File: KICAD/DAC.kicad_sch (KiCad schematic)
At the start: 34 parts, among them IC4 PCM5102AQPWRQ1, IC6 PCM5102AQPWRQ1

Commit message: clear
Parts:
- IC4, IC6: footprint Package_SO:TSSOP-20_4.4x6.5mm_P0.65mm -> footprints:PCM5102AQPWRQ1
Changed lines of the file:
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@@
 			)
 		)
-		(property "Footprint" "Package_SO:TSSOP-20_4.4x6.5mm_P0.65mm"
+		(property "Footprint" "footprints:PCM5102AQPWRQ1"
 			(at 101.6 47.32 0)
 			(hide yes)
@@
 			)
 		)
-		(property "Footprint" "Package_SO:TSSOP-20_4.4x6.5mm_P0.65mm"
+		(property "Footprint" "footprints:PCM5102AQPWRQ1"
 			(at 100.33 -6.02 0)
 			(hide yes)

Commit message: Verification PCM5102A
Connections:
- net GND: now also IC6.12 (SCK)
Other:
- note added: "c'est parfait mec, il manquait juste un fil entre SCK et GND sur un des PCM5102A"
- moved on the sheet: C54, C57, C58, C59, C60, C61, C62, C63, C64, C65, C66, C67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

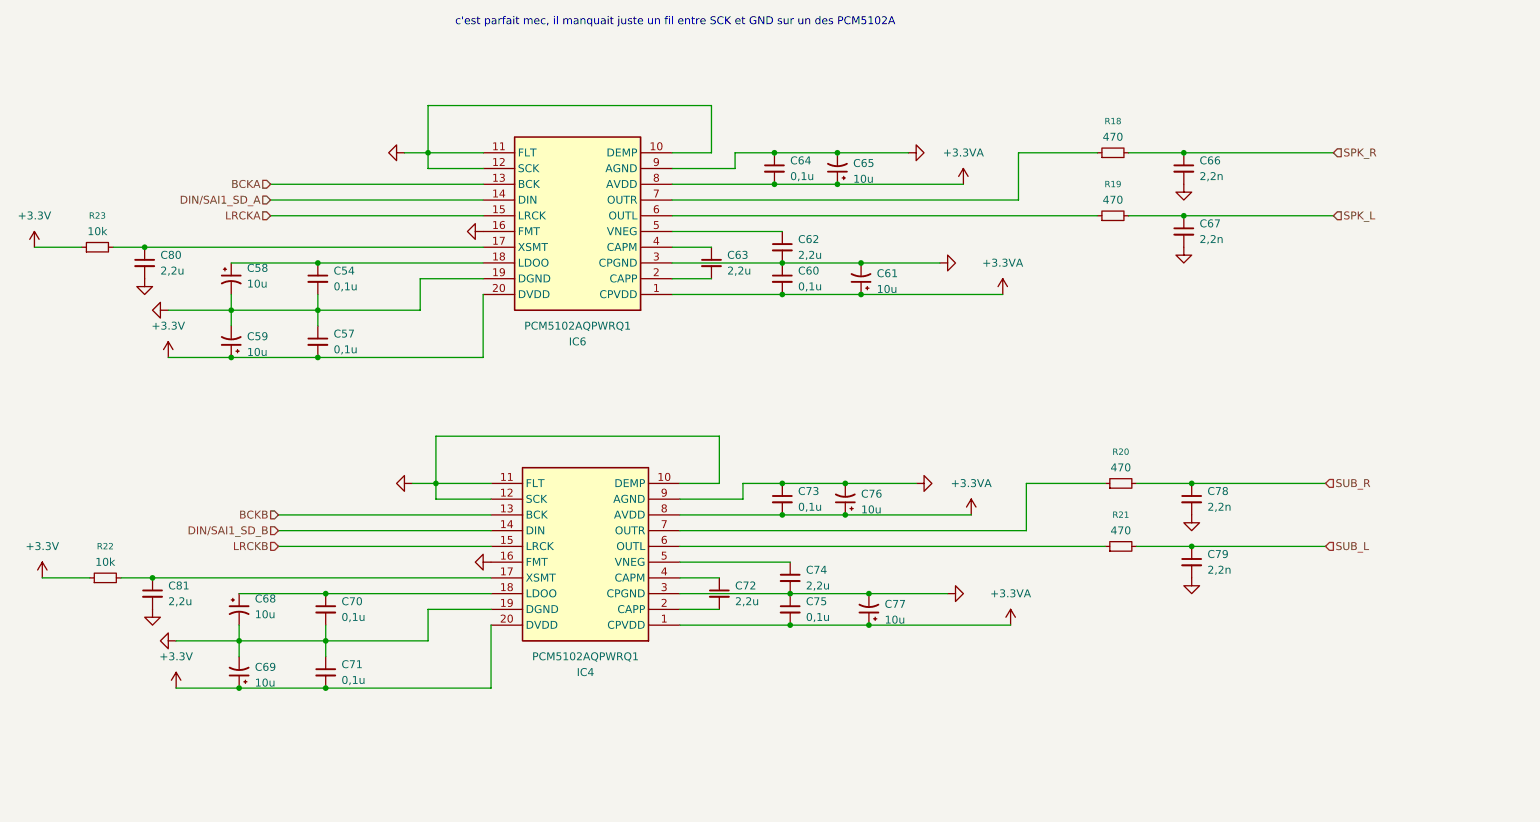
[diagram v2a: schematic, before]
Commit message: supression du subwoofer
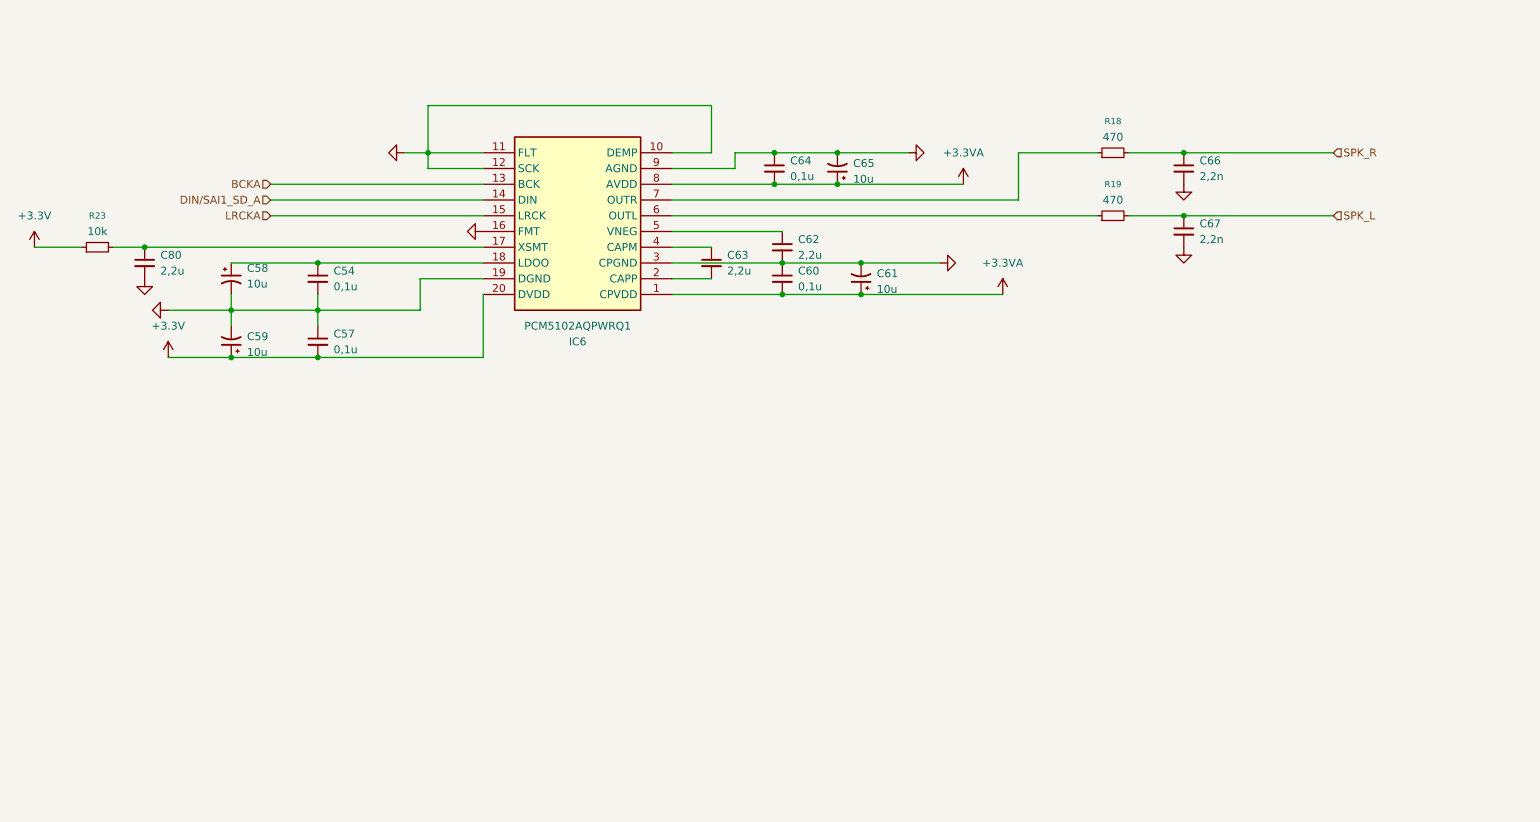
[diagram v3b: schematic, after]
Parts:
- removed C68, C69, C76, C77: 10u, symbol Device:C_Polarized_Small_US
- removed C70, C71, C73, C75: 0,1u, symbol Device:C_Small
- removed C72, C74, C81: 2,2u, symbol Device:C_Small
- removed C78, C79: 2,2n, symbol Device:C_Small
- removed IC4: PCM5102AQPWRQ1, footprints:PCM5102AQPWRQ1, symbol PCM5102AQPWRQ1:PCM5102AQPWRQ1
- removed R20, R21: 470, symbol Device:R_Small
- removed R22: 10k, symbol Device:R_Small
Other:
- note removed: "c'est parfait mec, il manquait juste un fil entre SCK et GND sur un des PCM5102A"

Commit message: mise en forme globale
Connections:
- net +3.3V renamed +3V3
- net BCKA renamed BCK
- net DIN/SAI1_SD_A renamed DIN
- net LRCKA renamed LRCK
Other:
- moved on the sheet: C54, C57, C58, C59, C60, C61, C62, C63, C64, C65, C66, C67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

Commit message: interface HM
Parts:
- added C68: 10u, symbol Device:C_Small
- added R20: 2.2, symbol Device:R_Small
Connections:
- net +3.3VA: now also C68.1, R20.2
- net +3V3: now also R20.1
- net GND: now also C68.2
- net BCK renamed I2S_BCK
- net DIN renamed I2S_DIN
- net LRCK renamed I2S_LRCK
